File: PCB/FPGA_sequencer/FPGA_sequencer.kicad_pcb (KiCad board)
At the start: 2 copper layers, 57 parts, among them J1 Conn_Coaxial, U1 ADA4940-2ACPZ-R7_a, U2 AD9648BCPZ-125, U3 DB3S406F0L, U4 DB3S406F0L, U5 AD8065ARTZ-R2, U6 MAX4564EKA+T

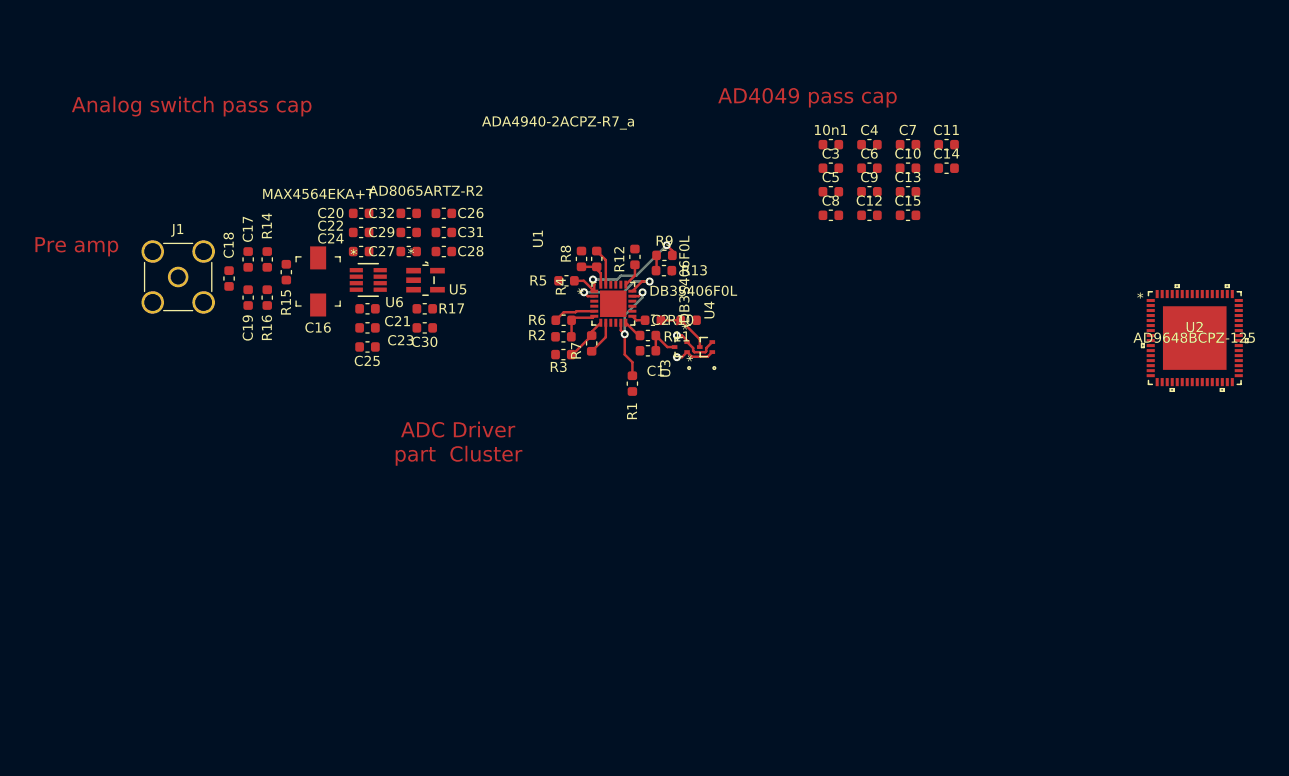
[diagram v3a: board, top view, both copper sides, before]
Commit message: Current Controller and GradientDriver_rev2
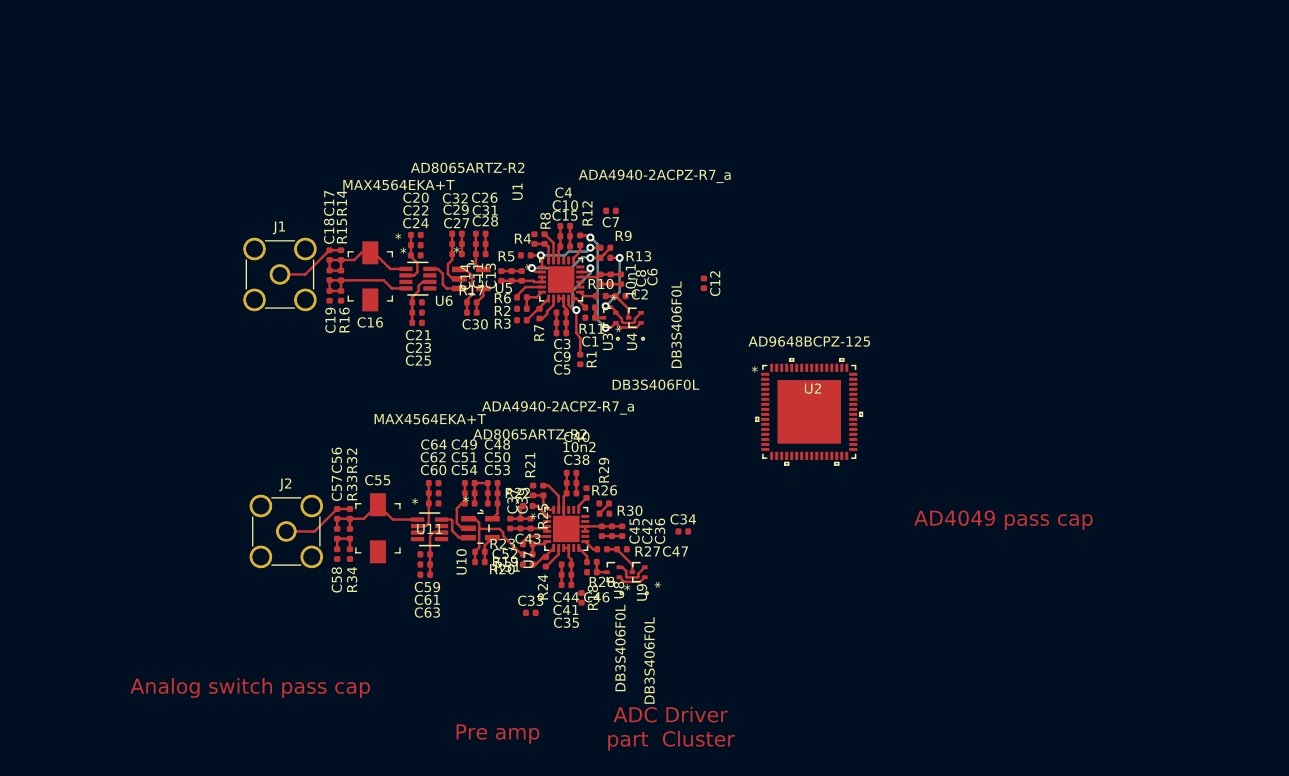
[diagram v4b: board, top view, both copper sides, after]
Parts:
- added 10n2: 0.1u, Capacitor_SMD:C_0402_1005Metric, F.Cu at (105.9, 58.4)
- added C33: 10u, Capacitor_SMD:C_0402_1005Metric, F.Cu at (101.9, 70.4)
- added C34: 10u, Capacitor_SMD:C_0402_1005Metric, F.Cu at (117.1, 62.2)
- added C35: 1u, Capacitor_SMD:C_0402_1005Metric, F.Cu at (105.4, 67.6)
- added C36: 1u, Capacitor_SMD:C_0402_1005Metric, F.Cu at (111.0, 62.2)
- added C37: 0.1u, Capacitor_SMD:C_0402_1005Metric, F.Cu at (99.8, 61.4)
- added C38: 0.1u, Capacitor_SMD:C_0402_1005Metric, F.Cu at (105.9, 56.4)
- added C39: 0.1u, Capacitor_SMD:C_0402_1005Metric, F.Cu at (100.8, 61.4)
- added C40: 0.1u, Capacitor_SMD:C_0402_1005Metric, F.Cu at (105.9, 57.4)
- added C41: 0.1u, Capacitor_SMD:C_0402_1005Metric, F.Cu at (105.4, 66.5)
- added C42: 0.1u, Capacitor_SMD:C_0402_1005Metric, F.Cu at (110.0, 62.2)
- added C43: 10n, Capacitor_SMD:C_0402_1005Metric, F.Cu at (101.9, 61.4)
- added C44: 10n, Capacitor_SMD:C_0402_1005Metric, F.Cu at (105.4, 65.5)
- added C45: 10n, Capacitor_SMD:C_0402_1005Metric, F.Cu at (109.0, 62.2)
- added C46: 22p, Capacitor_SMD:C_0402_1005Metric, F.Cu at (108.0, 66.3)
- added C47: 22p, Capacitor_SMD:C_0402_1005Metric, F.Cu at (111.0, 64.0)
- added C48: 1u, Capacitor_SMD:C_0402_1005Metric, F.Cu at (98.1, 57.4)
- added C49: 1u, Capacitor_SMD:C_0402_1005Metric, F.Cu at (95.8, 57.4)
- added C50: 0.1u, Capacitor_SMD:C_0402_1005Metric, F.Cu at (98.1, 58.4)
- added C51: 0.1u, Capacitor_SMD:C_0402_1005Metric, F.Cu at (95.8, 58.4)
- added C52: 150p, Capacitor_SMD:C_0402_1005Metric, F.Cu at (96.8, 64.3)
- added C53: 10n, Capacitor_SMD:C_0402_1005Metric, F.Cu at (98.1, 59.4)
- added C54: 10n, Capacitor_SMD:C_0402_1005Metric, F.Cu at (95.8, 59.4)
- added C55: C_Variable, Capacitor_SMD:C_Trimmer_Murata_TZB4-A, F.Cu at (86.6, 61.9)
- added C56: 33p, Capacitor_SMD:C_0402_1005Metric, F.Cu at (82.5, 60.5)
- added C57: 91p, Capacitor_SMD:C_0402_1005Metric, F.Cu at (82.5, 62.5)
- added C58: 1n, Capacitor_SMD:C_0402_1005Metric, F.Cu at (82.5, 64.5)
- added C59: 10n, Capacitor_SMD:C_0402_1005Metric, F.Cu at (91.3, 64.5)
- added C60: 10n, Capacitor_SMD:C_0402_1005Metric, F.Cu at (92.2, 59.4)
- added C61: 0.1u, Capacitor_SMD:C_0402_1005Metric, F.Cu at (91.3, 65.5)
- added C62: 0.1u, Capacitor_SMD:C_0402_1005Metric, F.Cu at (92.2, 58.4)
- added C63: 1u, Capacitor_SMD:C_0402_1005Metric, F.Cu at (91.3, 66.5)
- added C64: 1u, Capacitor_SMD:C_0402_1005Metric, F.Cu at (92.2, 57.4)
- added J2: Conn_Coaxial, Connector_Coaxial:SMA_Amphenol_132134-11_Vertical, F.Cu at (77.5, 62.2)
- added R18: 33, Resistor_SMD:R_0402_1005Metric, F.Cu at (106.9, 68.9)
- added R19: 2.2k, Resistor_SMD:R_0402_1005Metric, F.Cu at (101.6, 64.5)
- added R20: 2.2k, Resistor_SMD:R_0402_1005Metric, F.Cu at (101.6, 65.5)
- added R21: 6.34k, Resistor_SMD:R_0402_1005Metric, F.Cu at (102.1, 58.1)
- added R22: 6.34k, Resistor_SMD:R_0402_1005Metric, F.Cu at (101.6, 59.7)
- added R23: 3.9k, Resistor_SMD:R_0402_1005Metric, F.Cu at (101.6, 63.5)
- added R24: 3.9k, Resistor_SMD:R_0402_1005Metric, F.Cu at (103.4, 65.3)
- added R25: 4.99k, Resistor_SMD:R_0402_1005Metric, F.Cu at (103.1, 58.1)
- added R26: 4.99k, Resistor_SMD:R_0402_1005Metric, F.Cu at (109.2, 59.4)
- added R27: 100, Resistor_SMD:R_0402_1005Metric, F.Cu at (109.0, 64.0)
- added R28: 100, Resistor_SMD:R_0402_1005Metric, F.Cu at (108.0, 65.3)
- added R29: 4.99, Resistor_SMD:R_0402_1005Metric, F.Cu at (107.4, 58.4)
- added R30: 4.99, Resistor_SMD:R_0402_1005Metric, F.Cu at (109.2, 60.5)
- added R31: 10k, Resistor_SMD:R_0402_1005Metric, F.Cu at (96.8, 65.3)
- added R32: 820k, Resistor_SMD:R_0402_1005Metric, F.Cu at (83.8, 60.5)
- added R33: 820k, Resistor_SMD:R_0402_1005Metric, F.Cu at (83.8, 62.5)
- added R34: 820k, Resistor_SMD:R_0402_1005Metric, F.Cu at (83.8, 64.5)
- added U10: AD8065ARTZ-R2, FPGA_sequencer:AD8065ARTZ-R2, F.Cu at (96.9, 61.9)
- added U11: MAX4564EKA+T, FPGA_sequencer:MAX4564EKA&plus_T, F.Cu at (91.8, 62.0)
- added U7: ADA4940-2ACPZ-R7_a, FPGA_sequencer:ADA4940-2ACPZ-R7, F.Cu at (105.4, 62.0)
- added U8: DB3S406F0L, FPGA_sequencer:DB3S406F0L, F.Cu at (110.1, 66.3)
- added U9: DB3S406F0L, FPGA_sequencer:DB3S406F0L, F.Cu at (112.6, 66.3)
- 10n1, C1, C10, C11, C12, C13, C14, C15, C17, C18, C19, C2, C20, C21, C22, C23, C24, C25, C26, C27, C28, C29, C3, C30, C31, C32, C4, C5, C6, C7, C8, C9: footprint Capacitor_SMD:C_0603_1608Metric -> Capacitor_SMD:C_0402_1005Metric
- R1, R10, R11, R12, R13, R14, R15, R16, R17, R2, R3, R4, R5, R6, R7, R8, R9: footprint Resistor_SMD:R_0603_1608Metric -> Resistor_SMD:R_0402_1005Metric
- moved C14 45.7 mm to (98.9, 36.7), turned to 270 degrees
- moved C11 45.4 mm to (99.9, 36.7), turned to 270 degrees
- moved C13 39.5 mm to (101.0, 36.7), turned to 270 degrees
- moved U2 39.2 mm to (129.7, 50.3)
- moved C10 34.9 mm to (105.3, 32.8)
- moved C15 34.4 mm to (105.3, 33.8)
- moved C9 33.4 mm to (104.9, 41.4)
- moved C4 31.4 mm to (105.3, 31.8)
- moved C3 30.5 mm to (104.9, 40.4)
- moved C7 30.4 mm to (109.9, 30.2), turned to 180 degrees
- moved C5 30.4 mm to (104.9, 42.4)
- moved C6 27.2 mm to (110.9, 37.1), turned to 270 degrees
- moved 10n1 26.6 mm to (108.8, 37.1), turned to 270 degrees
- moved C8 22.9 mm to (109.9, 37.1), turned to 270 degrees
- moved C12 17.9 mm to (119.1, 37.5), turned to 270 degrees
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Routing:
- net -3V3: track 0.00 -> 19.8 mm
- net GNDA: track 0.00 -> 17.7 mm
- net +3V3: track 0.00 -> 17.5 mm
- net Net-(C16-Pad1): track 0.00 -> 11.8 mm
- net Net-(C55-Pad1): track 0.00 -> 11.3 mm
- net Net-(C18-Pad1): track 0.00 -> 11.2 mm
- net Net-(C52-Pad2): track 0.00 -> 10.9 mm
- net Net-(R12-Pad1): track 4.13 -> 14.9 mm, vias 1 -> 2
- net Net-(C56-Pad2): track 0.00 -> 7.28 mm
- net Net-(C17-Pad2): track 0.00 -> 7.10 mm
- net Net-(R13-Pad1): track 5.45 -> 11.4 mm, vias 1 -> 2
- net Net-(C49-Pad1): track 0.00 -> 5.88 mm
- net Net-(C27-Pad1): track 0.00 -> 5.54 mm
- net Net-(C30-Pad2): track 0.00 -> 5.43 mm
- net Net-(R5-Pad1): track 13.9 -> 8.52 mm
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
